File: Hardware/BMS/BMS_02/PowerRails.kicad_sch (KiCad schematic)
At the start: 55 parts, among them Q32 Q_DUAL_NMOS_PMOS, Q33 Q_DUAL_NMOS_PMOS, U12 TLX9185A(GBTPL,F, U2 LM2931-5.0_SO8, U3 TPS73633DBV, U4 LTC3638, U9 TPS2551-Q1

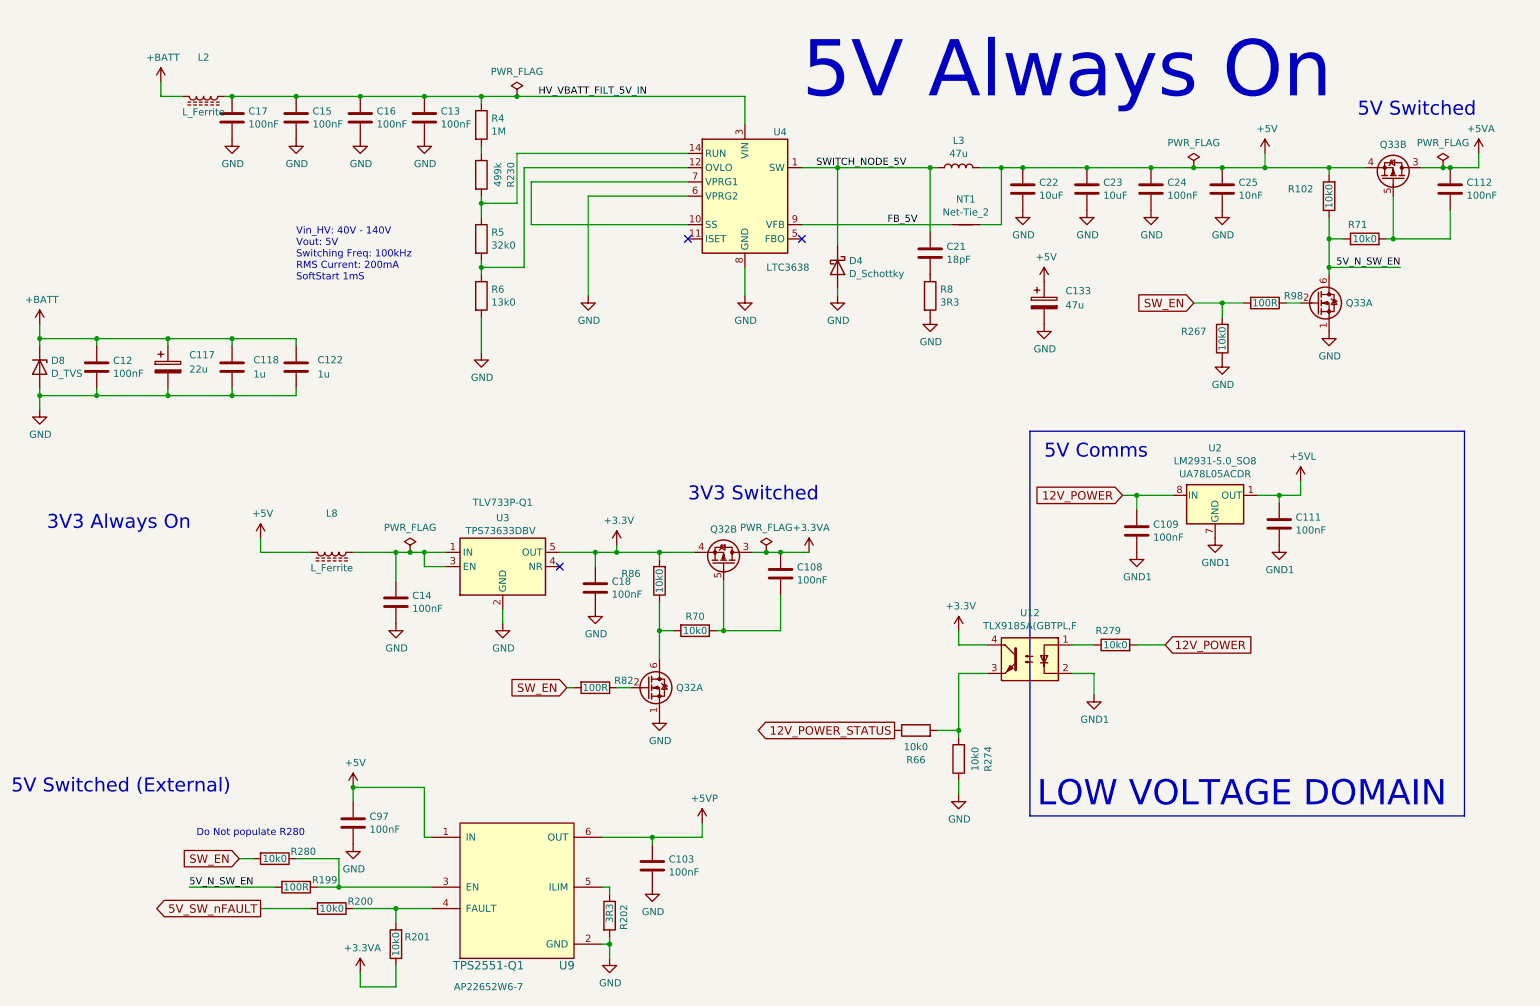
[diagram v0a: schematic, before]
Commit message: bms 02 build and code bring up. Board is built, bootloader is stable and uploads app flawlessly.
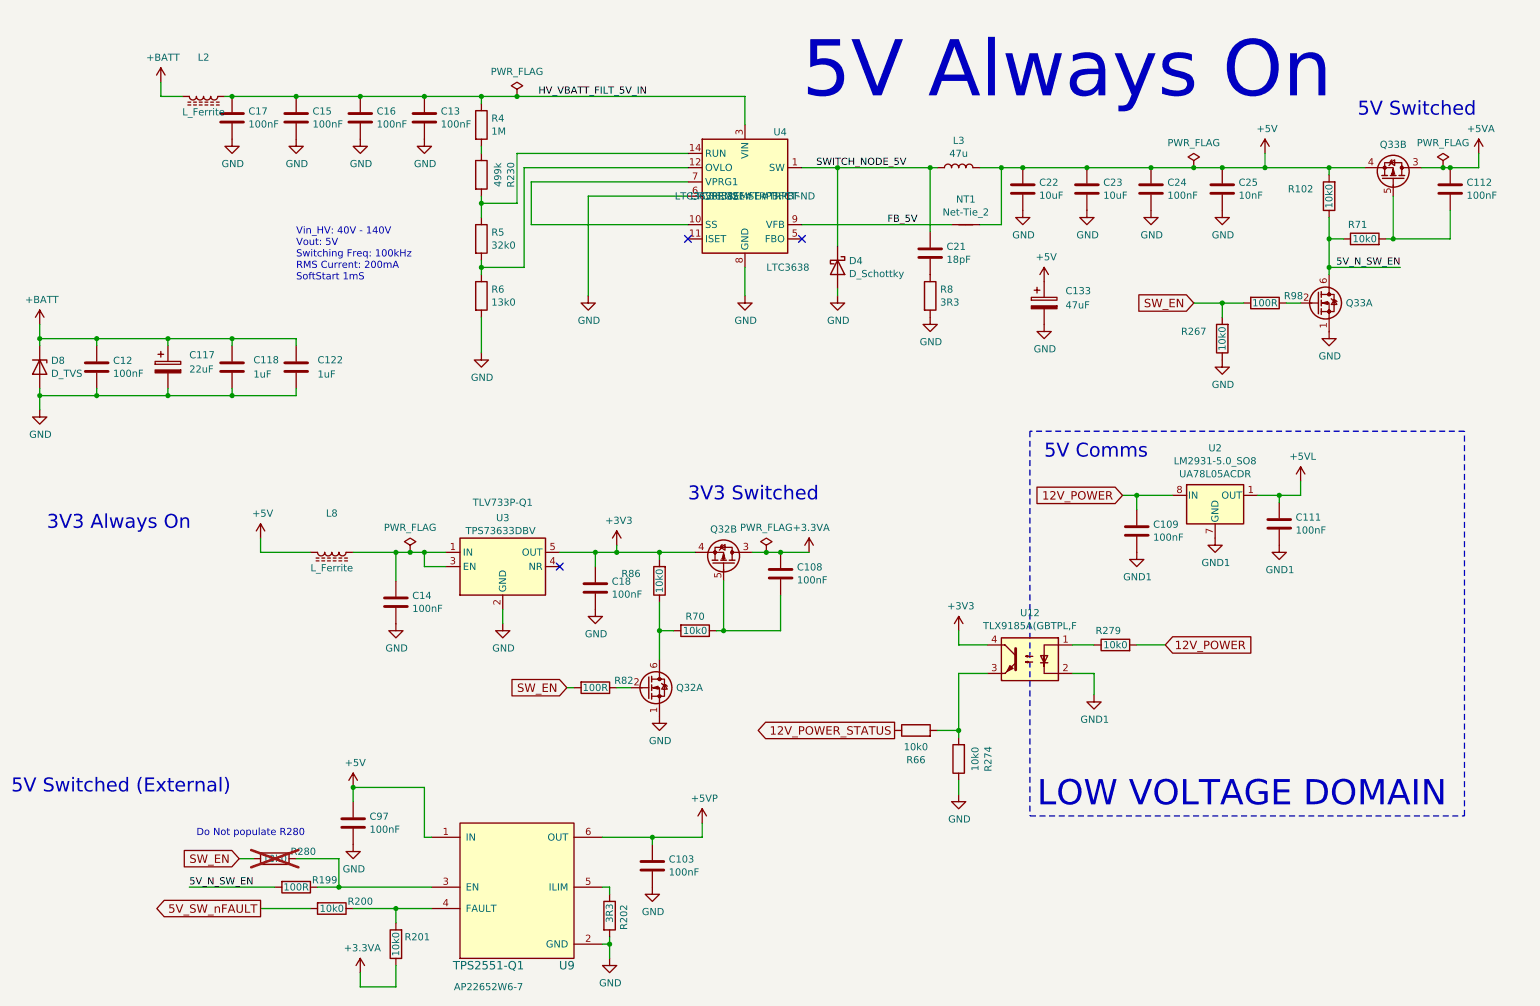
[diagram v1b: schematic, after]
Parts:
- C117: value 22u -> 22uF
- C118, C122: value 1u -> 1uF
- C133: value 47u -> 47uF
- NT1: now left out of the parts list
- R102, R200, R201, R267, R279, R4, R70, R71, R86: DNP < ... > -> (none)
- R280: DNP < ... > -> (none); now not fitted; now left out of the parts list
- U4: Digikey_PN (none) -> LTC3638EMSE#TRPBFCT-ND; MPN (none) -> LTC3638EMSE#TRPBF
